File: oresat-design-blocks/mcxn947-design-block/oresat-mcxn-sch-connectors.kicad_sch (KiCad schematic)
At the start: 49 parts, among them J1 BKUP-BATT, J2 USB_C_Receptacle_USB2.0_14P, J7 OreSat Debug, U1 MCXN947VKLT, U3 TPS62111RSA

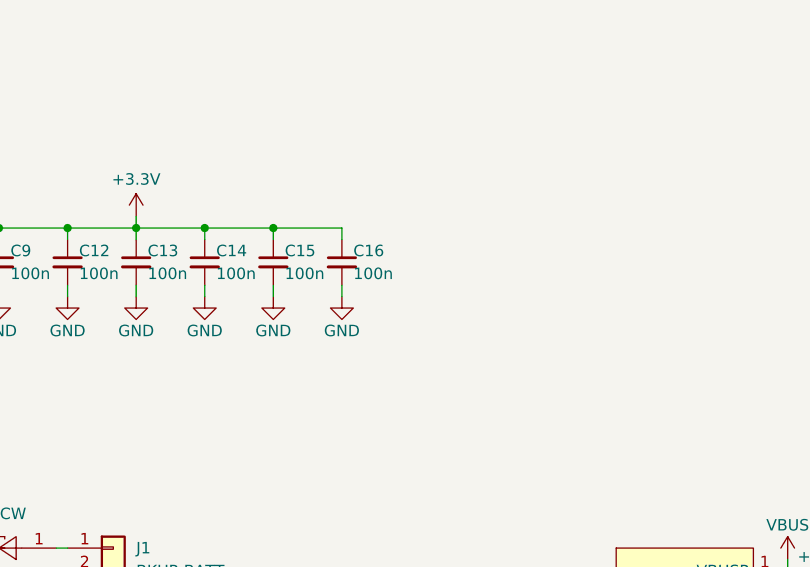
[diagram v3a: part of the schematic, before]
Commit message: Lots of DRC cleanup - why were there so many shorting errors?! Maybe this was never really checked. Added capacitor for bypass on MCXN pin.
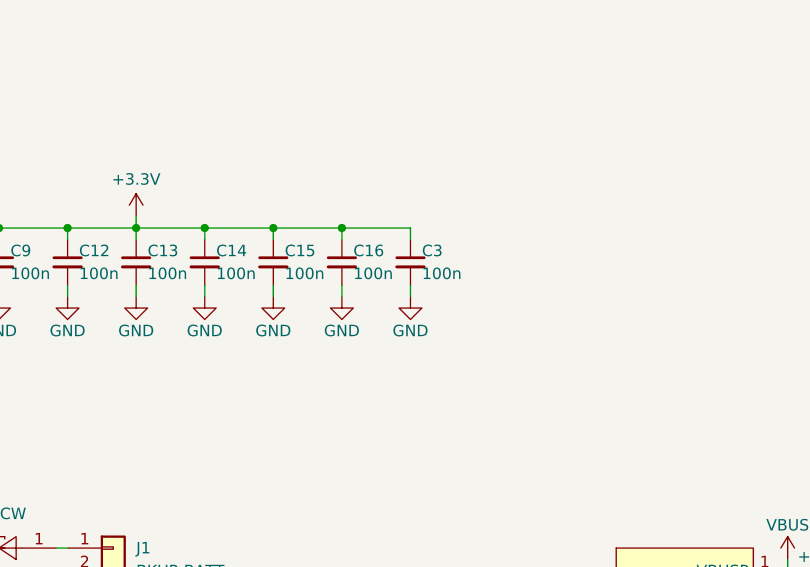
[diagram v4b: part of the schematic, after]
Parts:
- added C3: 100n, oresat-passives:0603-C-NOSILK, symbol Device:C_Small
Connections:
- net +3.3V: now also C3.1
- net GND: now also C3.2
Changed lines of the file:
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@@
 	)
 	(junction
+		(at 193.04 137.16)
+		(diameter 0)
+		(color 0 0 0 0)
+	)
+	(junction
 		(at 125.73 146.05)
 		(diameter 0)
@@
 	(wire
 		(pts
+			(xy 200.66 143.51) (xy 200.66 144.78)
+		)
+		(stroke
+			(width 0)
+			(type default)
+		)
+	)
+	(wire
+		(pts
 			(xy 63.5 146.05) (xy 63.5 147.32)
 		)
@@
 	(wire
 		(pts
+			(xy 200.66 137.16) (xy 200.66 138.43)
+		)
+		(stroke
+			(width 0)
+			(type default)
+		)
+	)
+	(wire
+		(pts
 			(xy 116.84 200.66) (xy 116.84 201.93)
 		)
@@
 	(wire
 		(pts
+			(xy 193.04 137.16) (xy 200.66 137.16)
+		)
+		(stroke
+			(width 0)
+			(type default)
+		)
+	)
+	(wire
+		(pts
 			(xy 162.56 137.16) (xy 170.18 137.16)
 		)
@@
 	(symbol
 		(lib_id "Device:C_Small")
+		(at 200.66 140.97 0)
+		(unit 1)
+		(exclude_from_sim no)
+		(in_bom yes)
+		(on_board yes)
+		(dnp no)
+		(property "Reference" "C3"
+			(at 201.93 139.7 0)
+			(effects
+				(font
+					(size 1.27 1.27)
+				)
+				(justify left)
+			)
+		)
+		(property "Value" "100n"
+			(at 201.93 142.24 0)
+			(effects
+				(font
+					(size 1.27 1.27)
+				)
+				(justify left)
+			)
+		)
+		(property "Footprint" "oresat-passives:0603-C-NOSILK"
+			(at 200.66 140.97 0)
+			(effects
+				(font
+					(size 1.27 1.27)
+				)
+				(hide yes)
+			)
+		)
+		(property "Datasheet" "https://search.murata.co.jp/Ceramy/image/img/A01X/G101/ENG/GRM188R72A104KA35-01.pdf"
+			(at 200.66 140.97 0)
+			(effects
+				(font
+					(size 1.27 1.27)
+				)
+				(hide yes)
+			)
+		)
+		(property "Description" "0.1 µF ±10% 100V Ceramic Capacitor X7R 0603 (1608 Metric)"
+			(at 200.66 140.97 0)
+			(effects
+				(font
+					(size 1.27 1.27)
+				)
+				(hide yes)
+			)
+		)
+		(property "MFR" "Murata Electronics"
+			(at 200.66 140.97 0)
+			(effects
+				(font
+					(size 1.27 1.27)
+				)
+				(hide yes)
+			)
+		)
+		(property "MPN" "GRM188R72A104KA35D"
+			(at 200.66 140.97 0)
+			(effects
+				(font
+					(size 1.27 1.27)
+				)
+				(hide yes)
+			)
+		)
+		(pin "2"
+		)
+		(pin "1"
+		)
+		(instances
+			(project "oresat-mcxn947"
+				(path "/52595c9f-7fa1-4e87-8727-2a72b29e4974/ee56f181-4a87-45c4-82f0-bfd072fe3741"
+					(reference "C3")
+					(unit 1)
+				)
+			)
+		)
+	)
+	(symbol
+		(lib_id "Device:C_Small")
 		(at 162.56 140.97 0)
 		(unit 1)
@@
 					(unit 1)
 				)
+			)
+		)
+	)
+	(symbol
+		(lib_id "power:GND")
+		(at 200.66 144.78 0)
+		(unit 1)
+		(exclude_from_sim no)
+		(in_bom yes)
+		(on_board yes)
+		(dnp no)
+		(property "Reference" "#PWR03"
+			(at 200.66 151.13 0)
+			(effects
+				(font
+					(size 1.27 1.27)
+				)
+				(hide yes)
+			)
+		)
+		(property "Value" "GND"
+			(at 200.66 148.59 0)
+			(effects
+				(font
+					(size 1.27 1.27)
+				)
+			)
+		)
+		(property "Footprint" ""
+			(at 200.66 144.78 0)
+			(effects
+				(font
+					(size 1.27 1.27)
+				)
+				(hide yes)
+			)
+		)
+		(property "Datasheet" ""
+			(at 200.66 144.78 0)
+			(effects
+				(font
+					(size 1.27 1.27)
+				)
+				(hide yes)
+			)
+		)
+		(property "Description" "Power symbol creates a global label with name \"GND\" , ground"
+			(at 200.66 144.78 0)
+			(effects
+				(font
+					(size 1.27 1.27)
+				)
+				(hide yes)
+			)
+		)
+		(pin "1"
+		)
+		(instances
+			(project "oresat-mcxn947"
+				(path "/52595c9f-7fa1-4e87-8727-2a72b29e4974/ee56f181-4a87-45c4-82f0-bfd072fe3741"
+					(reference "#PWR03")
+					(unit 1)
+				)

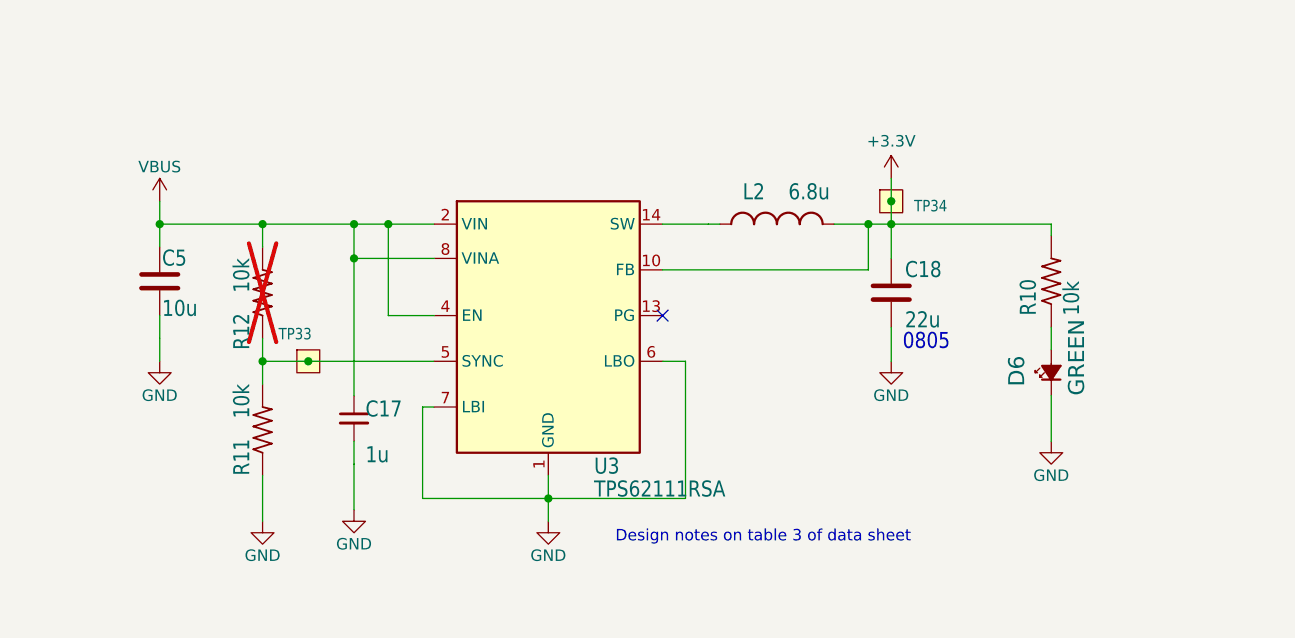
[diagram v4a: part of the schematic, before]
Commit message: Updated BOM with distributor part numbers, lots of double checking. Now truly version 1.1
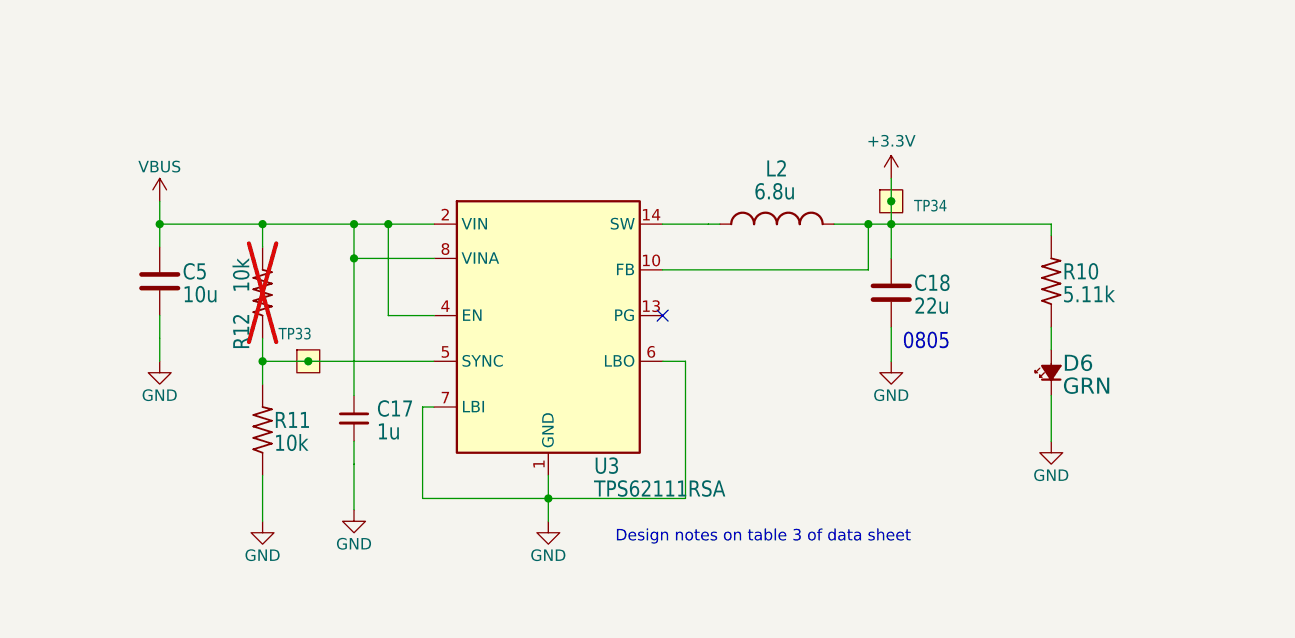
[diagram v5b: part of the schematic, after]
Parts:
- C1, C12, C13, C14, C15, C16, C2, C20, C3, C8, C9: DIS (none) -> DigiKey; DPN (none) -> 587-3472-1-ND; MFR Murata Electronics -> Taiyo Yuden; MPN GRM188R72A104KA35D -> TMK107BJ104KAHT
- C10: footprint oresat-passives:0603-C-NOSILK -> oresat-passives:0805-C-NOSILK; DIS (none) -> DigiKey; DPN (none) -> 445-12661-1-ND; MFR Murata Electronics -> TDK Corporation; MPN GCJ31CR71A685KA13L -> CGA4J1X5R1C685K125AC
- C11, C7: DIS (none) -> DigiKey; DPN (none) -> 587-4332-1-ND; MFR Murata Electronics -> Taiyo Yuden; MPN GRM188R61E475KE11D -> EMK107BBJ475KAHT
- C17: DIS Digi-Key -> DigiKey; DPN 311-1444-1-ND -> 587-3473-1-ND; MFR Murata Electronics -> Taiyo Yuden; MPN GRM185R61E105KA12J -> TMK107BJ105KAHT
- C18, L2, U3: DIS Digi-Key -> DigiKey
- C4: DIS (none) -> DigiKey; DPN (none) -> 587-3473-1-ND; MFR Murata Electronics -> Taiyo Yuden; MPN GRM185R61E105KA12J -> TMK107BJ105KAHT
- C5: DIS Digi-Key -> DigiKey; DPN 1276-6472-1-ND -> 490-18214-1-ND
- C6: DIS (none) -> DigiKey; DPN (none) -> 587-4929-1-ND; MFR Murata Electronics -> Taiyo Yuden; MPN GRM188R61E225KA12D -> TMK107BBJ225MAHT
- D1: DIS (none) -> DigiKey; DPN (none) -> 1727-2903-1-ND
- D6: value GREEN -> GRN; DIS Digi-Key -> DigiKey; DPN 511-1584-1-ND -> 732-4971-1-ND; MFR Rohm -> Wurth; MPN SML-E12M8WT86 -> 150060GS75000
- FB1: DIS (none) -> DigiKey; DPN (none) -> 1934-1472-1-ND
- J1: DIS (none) -> DigiKey; DPN (none) -> 2057-PH1-02-UA-ND
- J2: DIS (none) -> DigiKey; DPN (none) -> 2073-USB4105-GF-ACT-ND
- J7: DIS (none) -> DigiKey; DPN (none) -> A100287CT-ND
- L1: DIS (none) -> DigiKey; DPN (none) -> 118-SRP2012TMA-1R5MCT-ND
- R1, R2: DIS (none) -> DigiKey; DPN (none) -> RMCF0603FT5K11CT-ND
- R10: value 10k -> 5.11k; DIS Digi-Key -> DigiKey; DPN P2.7KDBCT-ND -> RMCF0603FT5K11CT-ND; MPN RMCF0603FT10K0 -> RMCF0603FT5K11
- R11: DIS Digi-Key -> DigiKey; DPN 1276-4275-1-ND -> RMCF0603FT10K0CT-ND
- R3: DIS (none) -> DigiKey; DPN (none) -> RMCF0603FT10K0CT-ND
- U1: DIS (none) -> Mouser; DPN (none) -> 771-MCXN947VKLT
